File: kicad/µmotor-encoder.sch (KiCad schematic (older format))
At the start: 6 parts, among them U401 AS5045B

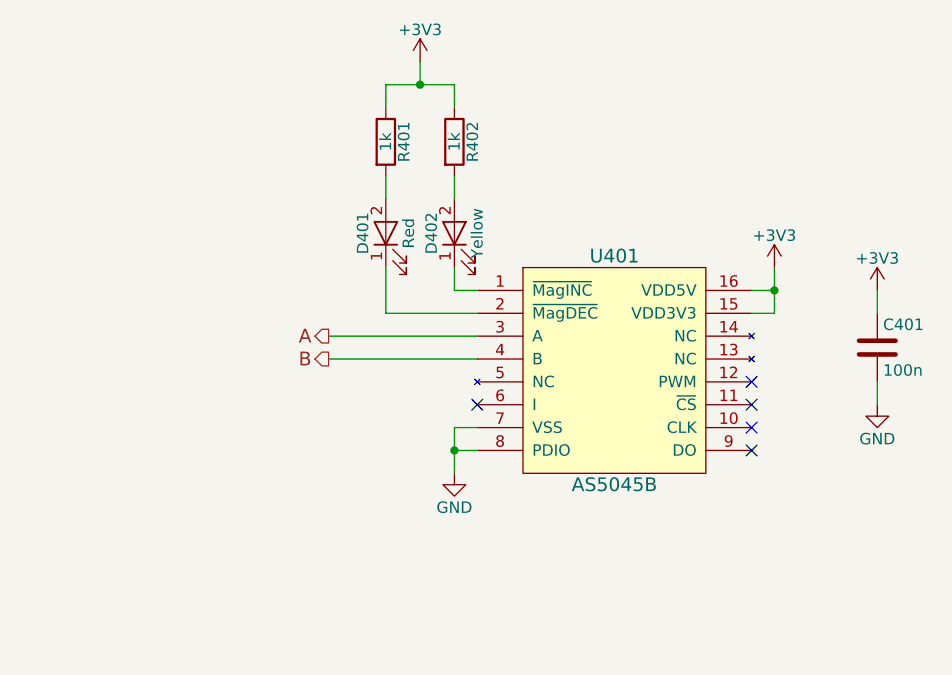
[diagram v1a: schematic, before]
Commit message: update µC pinout, motor driver, CubeMX, add 3V3 regulator and temperature sensor
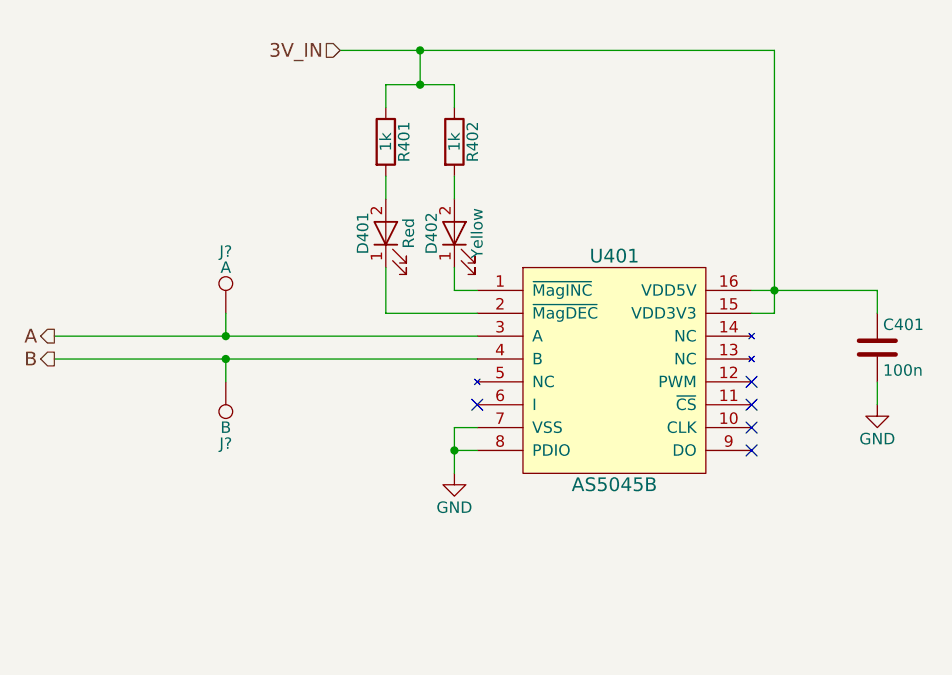
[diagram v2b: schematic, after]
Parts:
- added J?: A, symbol TEST_1P
- added J?: B, symbol TEST_1P
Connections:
- net A: now also J?.1
- net B: now also J?.1
- net +3V3 renamed 3V_IN
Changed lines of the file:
@@
 LIBS:drv8323s
 LIBS:FDMD82xx
+LIBS:ncp4623
+LIBS:TMP006
 LIBS:µmotor-cache
 EELAYER 25 0
@@
 $Descr A4 11693 8268
 encoding utf-8
-Sheet 3 6
+Sheet 2 6
 Title "µmotor - Micro Motor Controller"
 Date "2017-09-14"
@@
 	1    0    0    -1
 $EndComp
-$Comp
-L +3V3 #PWR016
-U 1 1 59BAD885
-P 6300 3350
-F 0 "#PWR016" H 6300 3200 50  0001 C CNN
-F 1 "+3V3" H 6300 3490 50  0000 C CNN
-F 2 "" H 6300 3350 50  0001 C CNN
-F 3 "" H 6300 3350 50  0001 C CNN
-	1    6300 3350
-	1    0    0    -1
-$EndComp
 Wire Wire Line
-	6300 3350 6300 3550
+	6300 2400 6300 3550
 Wire Wire Line
-	6300 3450 6200 3450
+	6200 3450 6750 3450
 Wire Wire Line
 	6300 3550 6200 3550
@@
 NoConn ~ 6200 3950
 NoConn ~ 6200 3850
-Text HLabel 4350 3650 0    60   Output ~ 0
+Text HLabel 3150 3650 0    60   Output ~ 0
 A
-Text HLabel 4350 3750 0    60   Output ~ 0
+Text HLabel 3150 3750 0    60   Output ~ 0
 B
 Wire Wire Line
-	4350 3750 5000 3750
+	3150 3750 5000 3750
 Wire Wire Line
-	5000 3650 4350 3650
+	3150 3650 5000 3650
 $Comp
 L C C401
@@
 F 3 "" H 6750 3700 50  0001 C CNN
 	1    6750 3700
-	1    0    0    -1
-$EndComp
-$Comp
-L +3V3 #PWR018
-U 1 1 59BADC81
-P 6750 3450
-F 0 "#PWR018" H 6750 3300 50  0001 C CNN
-F 1 "+3V3" H 6750 3590 50  0000 C CNN
-F 2 "" H 6750 3450 50  0001 C CNN
-F 3 "" H 6750 3450 50  0001 C CNN
-	1    6750 3450
 	1    0    0    -1
 $EndComp
@@
 	6750 3950 6750 3850
 Wire Wire Line
-	6750 3550 6750 3450
+	6750 3450 6750 3550
 Wire Wire Line
 	4900 3050 4900 2950
 Wire Wire Line
 	4600 3050 4600 2950
-$Comp
-L +3V3 #PWR020
-U 1 1 59BADF20
-P 4750 2450
-F 0 "#PWR020" H 4750 2300 50  0001 C CNN
-F 1 "+3V3" H 4750 2590 50  0000 C CNN
-F 2 "" H 4750 2450 50  0001 C CNN
-F 3 "" H 4750 2450 50  0001 C CNN
-	1    4750 2450
-	1    0    0    -1
-$EndComp
 Wire Wire Line
-	4750 2450 4750 2550
+	4750 2400 4750 2550
 Wire Wire Line
 	4600 2550 4900 2550
@@
 	4900 2550 4900 2650
 Connection ~ 4750 2550
+$Comp
+L TEST_1P J?
+U 1 1 5A76BD44
+P 3900 3550
+F 0 "J?" H 3900 3820 50  0000 C CNN
+F 1 "A" H 3900 3750 50  0000 C CNN
+F 2 "" H 4100 3550 50  0001 C CNN
+F 3 "" H 4100 3550 50  0001 C CNN
+	1    3900 3550
+	1    0    0    -1
+$EndComp
+$Comp
+L TEST_1P J?
+U 1 1 5A76BDAC
+P 3900 3850
+F 0 "J?" H 3900 4120 50  0000 C CNN
+F 1 "B" H 3900 4050 50  0000 C CNN
+F 2 "" H 4100 3850 50  0001 C CNN
+F 3 "" H 4100 3850 50  0001 C CNN
+	1    3900 3850
+	-1   0    0    1
+$EndComp
+Wire Wire Line
+	3900 3650 3900 3550
+Wire Wire Line
+	3900 3750 3900 3850
+Connection ~ 3900 3750
+Connection ~ 3900 3650
+Text HLabel 4400 2400 0    60   Input ~ 0
+3V_IN
+Wire Wire Line
+	4400 2400 6300 2400
+Connection ~ 4750 2400
 $EndSCHEMATC

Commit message: layout: components placed
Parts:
- added J203: 6V, Measurement_Point_Round-SMD-Pad_Smaller:Measurement_Point_Round-SMD-Pad_Smaller_0.75mm, symbol TEST_1P
- added J204: GND, Measurement_Point_Round-SMD-Pad_Smaller:Measurement_Point_Round-SMD-Pad_Smaller_0.75mm, symbol TEST_1P
- J201, J202: renamed from J?; footprint (none) -> Measurement_Point_Round-SMD-Pad_Smaller:Measurement_Point_Round-SMD-Pad_Smaller_0.75mm
- renumbered C401 to C201, D401 to D201, D402 to D202, R401 to R201, R402 to R202, U401 to U201
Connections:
- net GND: now also J204.1
- net 3V_IN renamed +3V3
- new net +6V: J203.1
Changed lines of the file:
@@
 LIBS:conn
 LIBS:linear
-LIBS:regul
-LIBS:74xx
-LIBS:cmos4000
-LIBS:adc-dac
-LIBS:memory
-LIBS:xilinx
-LIBS:microcontrollers
-LIBS:dsp
-LIBS:microchip
-LIBS:analog_switches
-LIBS:motorola
 LIBS:texas
-LIBS:intel
-LIBS:audio
 LIBS:interface
-LIBS:digital-audio
-LIBS:philips
-LIBS:display
-LIBS:cypress
-LIBS:siliconi
-LIBS:opto
-LIBS:atmel
 LIBS:contrib
 LIBS:valves
-LIBS:stm32
 LIBS:DRV8870
 LIBS:INA180A
@@
 LIBS:ncp4623
 LIBS:TMP006
+LIBS:stm32
 LIBS:µmotor-cache
 EELAYER 25 0
@@
 $EndDescr
 $Comp
-L AS5045B U401
+L AS5045B U201
 U 1 1 59BAD84A
 P 5600 3800
-F 0 "U401" H 5600 4300 60  0000 C CNN
+F 0 "U201" H 5600 4300 60  0000 C CNN
 F 1 "AS5045B" H 5600 3300 60  0000 C CNN
 F 2 "Housings_SSOP:SSOP-16_4.4x5.2mm_Pitch0.65mm" H 5650 3800 60  0001 C CNN
@@
 Connection ~ 6300 3450
 $Comp
-L GND #PWR017
+L GND #PWR07
 U 1 1 59BAD8B0
 P 4900 4250
-F 0 "#PWR017" H 4900 4000 50  0001 C CNN
+F 0 "#PWR07" H 4900 4000 50  0001 C CNN
 F 1 "GND" H 4900 4100 50  0000 C CNN
 F 2 "" H 4900 4250 50  0001 C CNN
@@
 NoConn ~ 5000 3950
 $Comp
-L LED D402
+L LED D202
 U 1 1 59BAD8DC
 P 4900 3200
-F 0 "D402" H 4900 3300 50  0000 C CNN
+F 0 "D202" H 4900 3300 50  0000 C CNN
 F 1 "Yellow" H 4900 3100 50  0000 C CNN
 F 2 "LEDs:LED_0603" H 4900 3200 50  0001 C CNN
@@
 $EndComp
 $Comp
-L LED D401
+L LED D201
 U 1 1 59BAD913
 P 4600 3200
-F 0 "D401" H 4600 3300 50  0000 C CNN
+F 0 "D201" H 4600 3300 50  0000 C CNN
 F 1 "Red" H 4600 3100 50  0000 C CNN
 F 2 "LEDs:LED_0603" H 4600 3200 50  0001 C CNN
@@
 	4900 3450 4900 3350
 $Comp
-L R R402
+L R R202
 U 1 1 59BAD94F
 P 4900 2800
-F 0 "R402" V 4980 2800 50  0000 C CNN
+F 0 "R202" V 4980 2800 50  0000 C CNN
 F 1 "1k" V 4900 2800 50  0000 C CNN
 F 2 "Resistors_SMD:R_0603" V 4830 2800 50  0001 C CNN
@@
 $EndComp
 $Comp
-L R R401
+L R R201
 U 1 1 59BAD99D
 P 4600 2800
-F 0 "R401" V 4680 2800 50  0000 C CNN
+F 0 "R201" V 4680 2800 50  0000 C CNN
 F 1 "1k" V 4600 2800 50  0000 C CNN
 F 2 "Resistors_SMD:R_0603" V 4530 2800 50  0001 C CNN
@@
 	3150 3650 5000 3650
 $Comp
-L C C401
+L C C201
 U 1 1 59BADC52
 P 6750 3700
-F 0 "C401" H 6775 3800 50  0000 L CNN
+F 0 "C201" H 6775 3800 50  0000 L CNN
 F 1 "100n" H 6775 3600 50  0000 L CNN
 F 2 "Capacitors_SMD:C_0603" H 6788 3550 50  0001 C CNN
@@
 $EndComp
 $Comp
-L GND #PWR019
+L GND #PWR08
 U 1 1 59BADC9E
 P 6750 3950
-F 0 "#PWR019" H 6750 3700 50  0001 C CNN
+F 0 "#PWR08" H 6750 3700 50  0001 C CNN
 F 1 "GND" H 6750 3800 50  0000 C CNN
 F 2 "" H 6750 3950 50  0001 C CNN
@@
 Connection ~ 4750 2550
 $Comp
-L TEST_1P J?
+L TEST_1P J201
 U 1 1 5A76BD44
 P 3900 3550
-F 0 "J?" H 3900 3820 50  0000 C CNN
+F 0 "J201" H 3900 3820 50  0000 C CNN
 F 1 "A" H 3900 3750 50  0000 C CNN
-F 2 "" H 4100 3550 50  0001 C CNN
+F 2 "Measurement_Point_Round-SMD-Pad_Smaller:Measurement_Point_Round-SMD-Pad_Smaller_0.75mm" H 4100 3550 50  0001 C CNN
 F 3 "" H 4100 3550 50  0001 C CNN
 	1    3900 3550
@@
 $EndComp
 $Comp
-L TEST_1P J?
+L TEST_1P J202
 U 1 1 5A76BDAC
 P 3900 3850
-F 0 "J?" H 3900 4120 50  0000 C CNN
+F 0 "J202" H 3900 4120 50  0000 C CNN
 F 1 "B" H 3900 4050 50  0000 C CNN
-F 2 "" H 4100 3850 50  0001 C CNN
+F 2 "Measurement_Point_Round-SMD-Pad_Smaller:Measurement_Point_Round-SMD-Pad_Smaller_0.75mm" H 4100 3850 50  0001 C CNN
 F 3 "" H 4100 3850 50  0001 C CNN
 	1    3900 3850
@@
 Connection ~ 3900 3750
 Connection ~ 3900 3650
-Text HLabel 4400 2400 0    60   Input ~ 0
-3V_IN
 Wire Wire Line
 	4400 2400 6300 2400
 Connection ~ 4750 2400
+$Comp
+L +3V3 #PWR09
+U 1 1 5A777D5D
+P 4400 2400
+F 0 "#PWR09" H 4400 2250 50  0001 C CNN
+F 1 "+3V3" H 4400 2540 50  0000 C CNN
+F 2 "" H 4400 2400 50  0001 C CNN
+F 3 "" H 4400 2400 50  0001 C CNN
+	1    4400 2400
+	0    -1   -1   0
+$EndComp
+$Comp
+L TEST_1P J203
+U 1 1 5A77A0C8
+P 3400 4750
+F 0 "J203" H 3400 5020 50  0000 C CNN
+F 1 "6V" H 3400 4950 50  0000 C CNN
+F 2 "Measurement_Point_Round-SMD-Pad_Smaller:Measurement_Point_Round-SMD-Pad_Smaller_0.75mm" H 3600 4750 50  0001 C CNN
+F 3 "" H 3600 4750 50  0001 C CNN
+	1    3400 4750
+	1    0    0    -1
+$EndComp
+$Comp
+L TEST_1P J204
+U 1 1 5A77A12B
+P 3600 4750
+F 0 "J204" H 3600 5020 50  0000 C CNN
+F 1 "GND" H 3600 4950 50  0000 C CNN
+F 2 "Measurement_Point_Round-SMD-Pad_Smaller:Measurement_Point_Round-SMD-Pad_Smaller_0.75mm" H 3800 4750 50  0001 C CNN
+F 3 "" H 3800 4750 50  0001 C CNN
+	1    3600 4750
+	1    0    0    -1
+$EndComp
+$Comp
+L +6V #PWR010
+U 1 1 5A77A32F
+P 3400 4850
+F 0 "#PWR010" H 3400 4700 50  0001 C CNN
+F 1 "+6V" H 3400 4990 50  0000 C CNN
+F 2 "" H 3400 4850 50  0001 C CNN
+F 3 "" H 3400 4850 50  0001 C CNN
+	1    3400 4850
+	-1   0    0    1
+$EndComp
+$Comp
+L GND #PWR011
+U 1 1 5A77A357
+P 3600 4850
+F 0 "#PWR011" H 3600 4600 50  0001 C CNN
+F 1 "GND" H 3600 4700 50  0000 C CNN
+F 2 "" H 3600 4850 50  0001 C CNN
+F 3 "" H 3600 4850 50  0001 C CNN
+	1    3600 4850
+	1    0    0    -1
+$EndComp
+Wire Wire Line
+	3600 4850 3600 4750
+Wire Wire Line
+	3400 4750 3400 4850
 $EndSCHEMATC
